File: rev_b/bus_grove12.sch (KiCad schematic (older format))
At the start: 57 parts, among them J1 TERMINATE_JUMPER, J2 LED_CONN_2X2, SW1 MJTP1243, U1 LM2940, U2 74HCT08, U3 MCP2562, U4 74HCT03, U5 ATMEGA328_DIP28, X1 16MHz

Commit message: Rev. B is ready.
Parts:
- C5: value 1uF -> .1uF
- N2: footprint bus_grove12:Pin_Header_Straight_1x06 -> ~
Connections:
- net GND: no longer H1.1 (GND), H2.1 (GND), H3.1 (GND), H4.1 (GND)
- net at R9.2, U4.12, U4.13: now also C7.1, R10.1
- no-connect marks 7 -> 11
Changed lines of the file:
@@
 Sheet 1 2
 Title "Bus Grove 12"
-Date "Sun 02 Nov 2014"
-Rev "A"
+Date "Mon 09 Feb 2015"
+Rev "B"
 Comp ""
 Comment1 ""
@@
 F 0 "N2" H 1050 8100 50  0000 C CNN
 F 1 "FTDI_HEADER" H 1150 7275 50  0000 C CNN
-F 2 "bus_grove12:Pin_Header_Straight_1x06" H 1150 7500 60  0001 C CNN
+F 2 "~" H 1150 7500 60  0000 C CNN
 F 3 "" H 1150 7500 60  0000 C CNN
 	1    1150 7500
@@
 P 4200 6950
 F 0 "C5" H 4260 7010 50  0000 L CNN
-F 1 "1uF" H 4260 6880 50  0000 L CNN
+F 1 ".1uF" H 4260 6880 50  0000 L CNN
 F 2 "bus_grove12:Capacitor4x3RM2-5_RevB" H 4238 6800 30  0001 C CNN
 F 3 "" H 4200 6950 60  0000 C CNN
@@
 	1800 6950 1800 7350
 Wire Wire Line
-	1600 7800 5300 7800
-Wire Wire Line
 	1800 7750 1800 7800
 Connection ~ 1800 7800
@@
 	5100 7400 5000 7400
 Connection ~ 5100 6950
-Wire Wire Line
-	5200 6600 5200 7800
-Wire Wire Line
-	5200 6600 5300 6600
-Wire Wire Line
-	5300 7000 5200 7000
-Connection ~ 5200 7000
-Wire Wire Line
-	5300 7400 5200 7400
-Connection ~ 5200 7400
-Connection ~ 5200 7800
 Wire Wire Line
 	4400 7400 4000 7400
@@
 Wire Wire Line
 	5600 6100 5600 5900
+Connection ~ 5900 1400
+Wire Wire Line
+	1600 7800 4000 7800
+NoConn ~ 5300 6600
+NoConn ~ 5300 7000
+NoConn ~ 5300 7400
+NoConn ~ 5300 7800
 $EndSCHEMATC

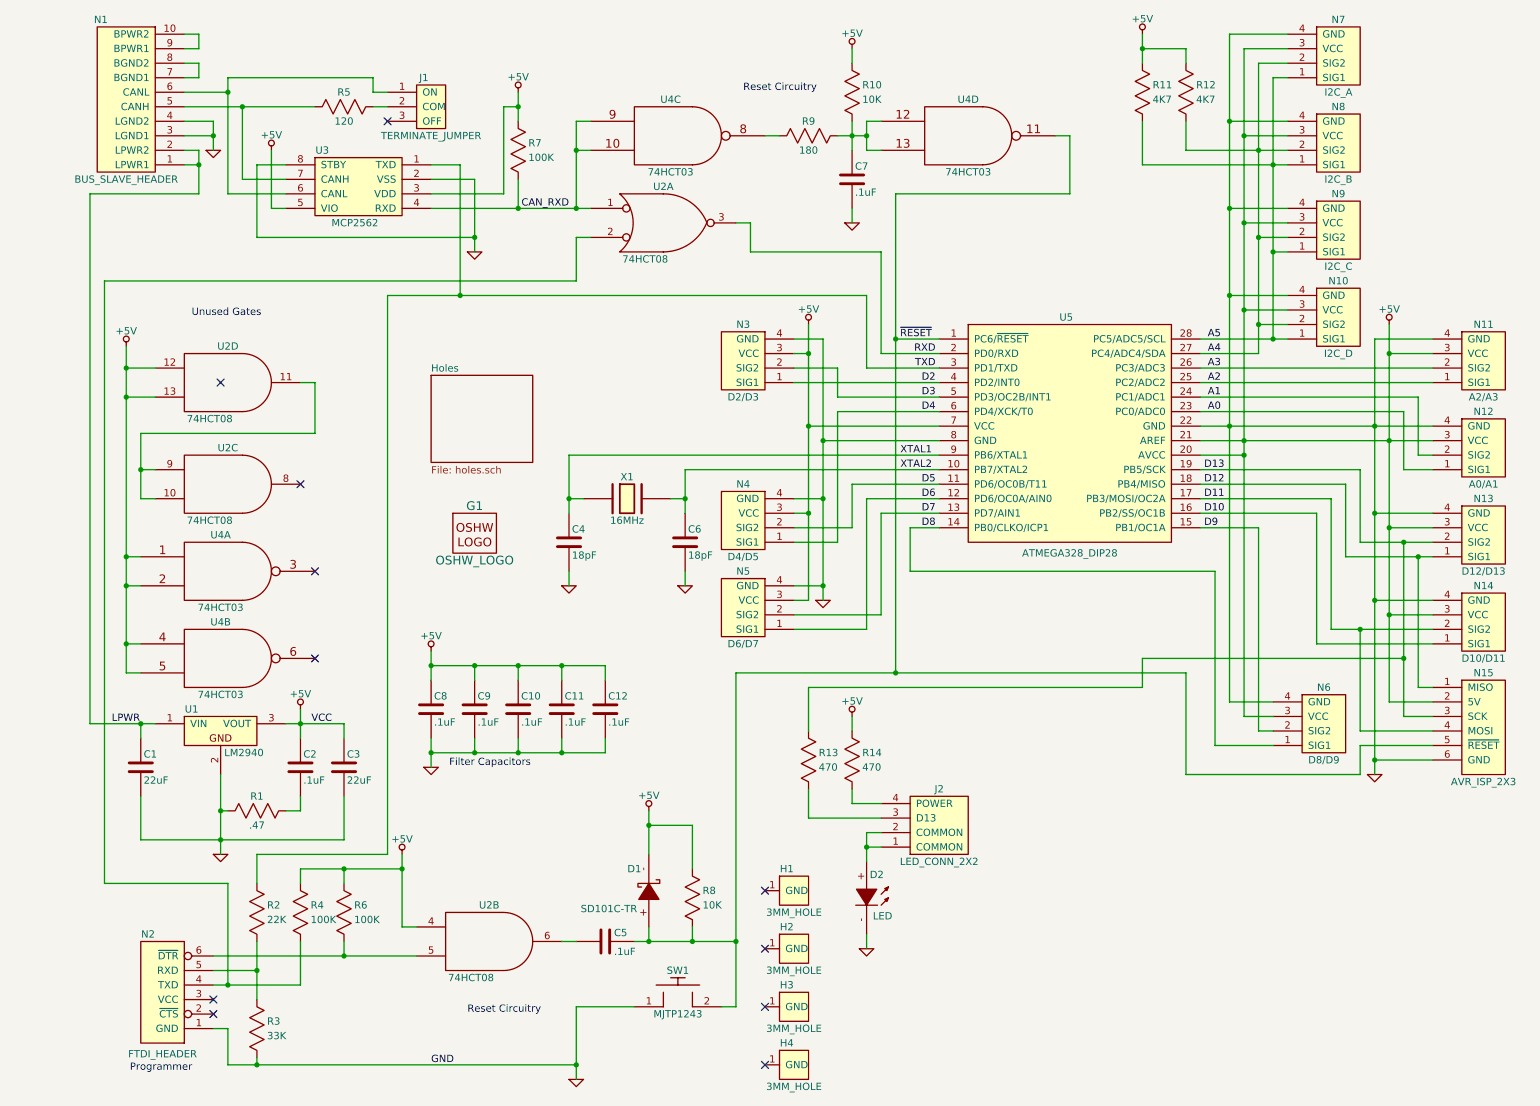
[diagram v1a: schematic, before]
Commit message: Split 22uF capacitor into tantalum and aluminum.
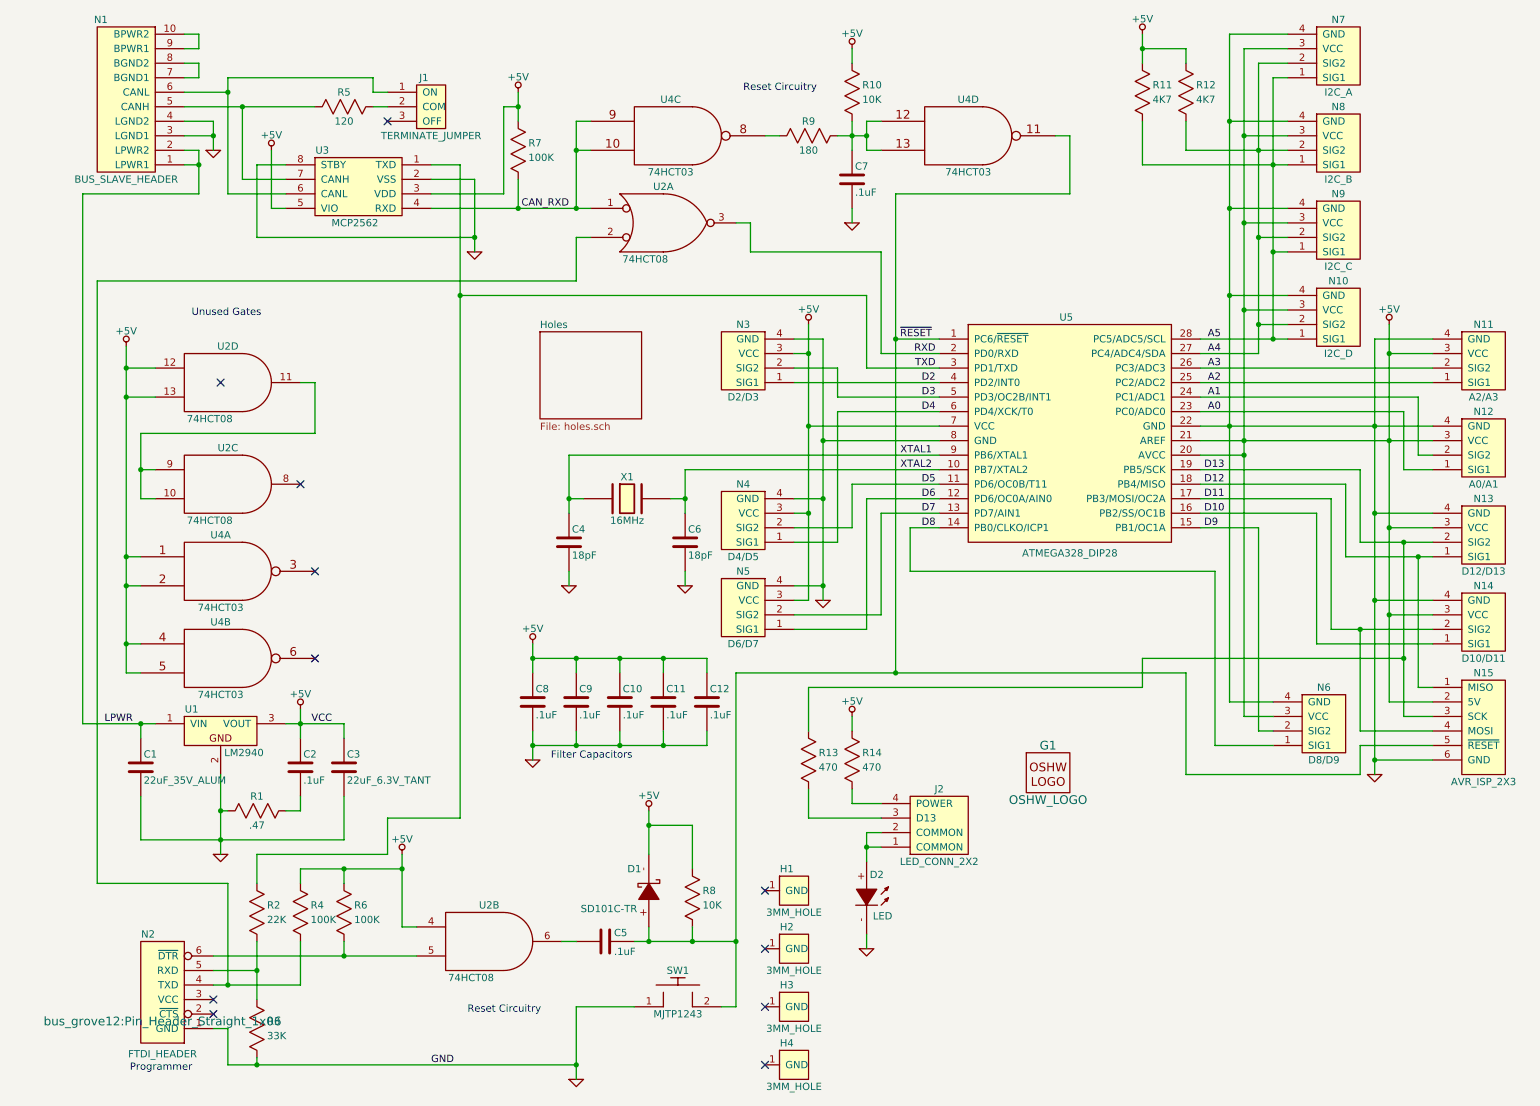
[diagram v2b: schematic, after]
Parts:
- C1: value 22uF -> 22uF_35V_ALUM
- C3: value 22uF -> 22uF_6.3V_TANT
- N2: footprint ~ -> bus_grove12:Pin_Header_Straight_1x06
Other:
- moved on the sheet: C10, C11, C12, C8, C9, G1
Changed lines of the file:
@@
 L OSHW_LOGO G1
 U 1 1 53AA4798
-P 3300 4150
-F 0 "G1" H 3300 4350 60  0000 C CNN
-F 1 "OSHW_LOGO" H 3300 3975 60  0000 C CNN
-F 2 "bus_grove12:OSHW_LOGO_400mil" H 3300 4150 60  0001 C CNN
-F 3 "" H 3300 4150 60  0000 C CNN
-	1    3300 4150
+P 7250 5800
+F 0 "G1" H 7250 6000 60  0000 C CNN
+F 1 "OSHW_LOGO" H 7250 5625 60  0000 C CNN
+F 2 "bus_grove12:OSHW_LOGO_400mil" H 7250 5800 60  0001 C CNN
+F 3 "" H 7250 5800 60  0000 C CNN
+	1    7250 5800
 	1    0    0    -1
 $EndComp
@@
 F 0 "N2" H 1050 8100 50  0000 C CNN
 F 1 "FTDI_HEADER" H 1150 7275 50  0000 C CNN
-F 2 "~" H 1150 7500 60  0000 C CNN
+F 2 "bus_grove12:Pin_Header_Straight_1x06" H 1150 7500 60  0000 C CNN
 F 3 "" H 1150 7500 60  0000 C CNN
 	1    1150 7500
@@
 P 1000 5750
 F 0 "C1" H 1020 5840 50  0000 L CNN
-F 1 "22uF" H 1020 5660 50  0000 L CNN
+F 1 "22uF_35V_ALUM" H 1020 5660 50  0000 L CNN
 F 2 "bus_grove12:Capacitor3MMDiscRM2.5" H 1038 5600 30  0001 C CNN
 F 3 "" H 1000 5750 60  0000 C CNN
@@
 P 2400 5750
 F 0 "C3" H 2420 5840 50  0000 L CNN
-F 1 "22uF" H 2420 5660 50  0000 L CNN
+F 1 "22uF_6.3V_TANT" H 2420 5660 50  0000 L CNN
 F 2 "bus_grove12:Capacitor3MMDiscRM2.5" H 2438 5600 30  0001 C CNN
 F 3 "" H 2400 5750 60  0000 C CNN
@@
 L C_VERT C8
 U 1 1 53EA3930
-P 3000 5350
-F 0 "C8" H 3020 5440 50  0000 L CNN
-F 1 ".1uF" H 3020 5260 50  0000 L CNN
-F 2 "bus_grove12:Capacitor4x3RM2-5_RevB" H 3038 5200 30  0001 C CNN
-F 3 "" H 3000 5350 60  0000 C CNN
-	1    3000 5350
+P 3700 5300
+F 0 "C8" H 3720 5390 50  0000 L CNN
+F 1 ".1uF" H 3720 5210 50  0000 L CNN
+F 2 "bus_grove12:Capacitor4x3RM2-5_RevB" H 3738 5150 30  0001 C CNN
+F 3 "" H 3700 5300 60  0000 C CNN
+	1    3700 5300
 	1    0    0    -1
 $EndComp
@@
 L C_VERT C9
 U 1 1 53EA3BB3
-P 3300 5350
-F 0 "C9" H 3320 5440 50  0000 L CNN
-F 1 ".1uF" H 3320 5260 50  0000 L CNN
-F 2 "bus_grove12:Capacitor4x3RM2-5_RevB" H 3338 5200 30  0001 C CNN
-F 3 "" H 3300 5350 60  0000 C CNN
-	1    3300 5350
+P 4000 5300
+F 0 "C9" H 4020 5390 50  0000 L CNN
+F 1 ".1uF" H 4020 5210 50  0000 L CNN
+F 2 "bus_grove12:Capacitor4x3RM2-5_RevB" H 4038 5150 30  0001 C CNN
+F 3 "" H 4000 5300 60  0000 C CNN
+	1    4000 5300
 	1    0    0    -1
 $EndComp
@@
 L C_VERT C10
 U 1 1 53EA3C1E
-P 3600 5350
-F 0 "C10" H 3620 5440 50  0000 L CNN
-F 1 ".1uF" H 3620 5260 50  0000 L CNN
-F 2 "bus_grove12:Capacitor4x3RM2-5_RevB" H 3638 5200 30  0001 C CNN
-F 3 "" H 3600 5350 60  0000 C CNN
-	1    3600 5350
+P 4300 5300
+F 0 "C10" H 4320 5390 50  0000 L CNN
+F 1 ".1uF" H 4320 5210 50  0000 L CNN
+F 2 "bus_grove12:Capacitor4x3RM2-5_RevB" H 4338 5150 30  0001 C CNN
+F 3 "" H 4300 5300 60  0000 C CNN
+	1    4300 5300
 	1    0    0    -1
 $EndComp
@@
 L C_VERT C11
 U 1 1 53EA3C8A
-P 3900 5350
-F 0 "C11" H 3920 5440 50  0000 L CNN
-F 1 ".1uF" H 3920 5260 50  0000 L CNN
-F 2 "bus_grove12:Capacitor4x3RM2-5_RevB" H 3938 5200 30  0001 C CNN
-F 3 "" H 3900 5350 60  0000 C CNN
-	1    3900 5350
+P 4600 5300
+F 0 "C11" H 4620 5390 50  0000 L CNN
+F 1 ".1uF" H 4620 5210 50  0000 L CNN
+F 2 "bus_grove12:Capacitor4x3RM2-5_RevB" H 4638 5150 30  0001 C CNN
+F 3 "" H 4600 5300 60  0000 C CNN
+	1    4600 5300
 	1    0    0    -1
 $EndComp
@@
 L +5V #PWR012
 U 1 1 53EA3CF1
-P 3000 4950
-F 0 "#PWR012" H 3000 5040 20  0001 C CNN
-F 1 "+5V" H 3000 5055 50  0000 C CNN
-F 2 "" H 3000 4950 60  0000 C CNN
-F 3 "" H 3000 4950 60  0000 C CNN
-	1    3000 4950
+P 3700 4900
+F 0 "#PWR012" H 3700 4990 20  0001 C CNN
+F 1 "+5V" H 3700 5005 50  0000 C CNN
+F 2 "" H 3700 4900 60  0000 C CNN
+F 3 "" H 3700 4900 60  0000 C CNN
+	1    3700 4900
 	1    0    0    -1
 $EndComp
@@
 L GND #PWR013
 U 1 1 53EA3DE7
-P 3000 5750
-F 0 "#PWR013" H 3000 5750 30  0001 C CNN
-F 1 "GND" H 3000 5680 30  0001 C CNN
-F 2 "" H 3000 5750 60  0000 C CNN
-F 3 "" H 3000 5750 60  0000 C CNN
-	1    3000 5750
-	1    0    0    -1
-$EndComp
-Text Notes 3125 5750 0    50   ~ 0
+P 3700 5700
+F 0 "#PWR013" H 3700 5700 30  0001 C CNN
+F 1 "GND" H 3700 5630 30  0001 C CNN
+F 2 "" H 3700 5700 60  0000 C CNN
+F 3 "" H 3700 5700 60  0000 C CNN
+	1    3700 5700
+	1    0    0    -1
+$EndComp
+Text Notes 3825 5700 0    50   ~ 0
 Filter Capacitors
 Text Notes 3250 7450 0    50   ~ 0
@@
 Text Notes 925  7850 0    50   ~ 0
 Programmer
-Text Label 800  5450 0    50   ~ 0
+Text Label 750  5450 0    50   ~ 0
 LPWR
 Text Label 6475 3200 2    50   ~ 0
@@
 L C_VERT C12
 U 1 1 53F15832
-P 4200 5350
-F 0 "C12" H 4220 5440 50  0000 L CNN
-F 1 ".1uF" H 4220 5260 50  0000 L CNN
-F 2 "bus_grove12:Capacitor4x3RM2-5_RevB" H 4238 5200 30  0001 C CNN
-F 3 "" H 4200 5350 60  0000 C CNN
-	1    4200 5350
+P 4900 5300
+F 0 "C12" H 4920 5390 50  0000 L CNN
+F 1 ".1uF" H 4920 5210 50  0000 L CNN
+F 2 "bus_grove12:Capacitor4x3RM2-5_RevB" H 4938 5150 30  0001 C CNN
+F 3 "" H 4900 5300 60  0000 C CNN
+	1    4900 5300
 	1    0    0    -1
 $EndComp
@@
 $EndComp
 $Sheet
-S 3000 3050 700  600
+S 3750 2750 700  600
 U 545698AF
 F0 "Holes" 50
@@
 Connection ~ 1000 5450
 Wire Wire Line
-	650  5450 1100 5450
+	600  5450 1100 5450
 Wire Wire Line
 	1000 5550 1000 5450
@@
 Connection ~ 1400 1600
 Wire Wire Line
-	650  1800 650  5450
-Wire Wire Line
-	1400 1800 650  1800
+	600  1800 600  5450
+Wire Wire Line
+	1400 1800 600  1800
 Connection ~ 1500 1400
 Wire Wire Line
@@
 	1600 7250 1600 6550
 Wire Wire Line
-	1600 6550 750  6550
-Wire Wire Line
-	750  6550 750  2400
-Wire Wire Line
-	750  2400 4000 2400
+	1600 6550 700  6550
+Wire Wire Line
+	700  6550 700  2400
+Wire Wire Line
+	700  2400 4000 2400
 Wire Wire Line
 	2100 6550 2100 6450
@@
 Wire Wire Line
 	2800 6850 2900 6850
-Wire Wire Line
-	2700 2500 2700 6350
 Wire Wire Line
 	2700 6350 1800 6350
@@
 	1800 1600 1800 2100
 Wire Wire Line
-	3000 4950 3000 5150
-Wire Wire Line
-	3000 5050 4200 5050
-Wire Wire Line
-	3900 5050 3900 5150
-Connection ~ 3000 5050
-Wire Wire Line
-	3600 5150 3600 5050
-Connection ~ 3600 5050
-Wire Wire Line
-	3300 5150 3300 5050
-Connection ~ 3300 5050
-Wire Wire Line
-	3000 5550 3000 5750
-Wire Wire Line
-	3000 5650 4200 5650
-Wire Wire Line
-	3900 5650 3900 5550
-Connection ~ 3000 5650
-Wire Wire Line
-	3600 5550 3600 5650
-Connection ~ 3600 5650
-Wire Wire Line
-	3300 5550 3300 5650
-Connection ~ 3300 5650
+	3700 4900 3700 5100
+Wire Wire Line
+	3700 5000 4900 5000
+Wire Wire Line
+	4600 5000 4600 5100
+Connection ~ 3700 5000
+Wire Wire Line
+	4300 5100 4300 5000
+Connection ~ 4300 5000
+Wire Wire Line
+	4000 5100 4000 5000
+Connection ~ 4000 5000
+Wire Wire Line
+	3700 5500 3700 5700
+Wire Wire Line
+	3700 5600 4900 5600
+Wire Wire Line
+	4600 5600 4600 5500
+Connection ~ 3700 5600
+Wire Wire Line
+	4300 5500 4300 5600
+Connection ~ 4300 5600
+Wire Wire Line
+	4000 5500 4000 5600
+Connection ~ 4000 5600
 Wire Wire Line
 	1300 1000 1400 1000
@@
 	2100 7250 2100 6950
 Wire Wire Line
-	4200 5050 4200 5150
-Connection ~ 3900 5050
-Wire Wire Line
-	4200 5650 4200 5550
-Connection ~ 3900 5650
-Wire Wire Line
-	3200 1600 3200 2500
+	4900 5000 4900 5100
+Connection ~ 4600 5000
+Wire Wire Line
+	4900 5600 4900 5500
+Connection ~ 4600 5600
+Wire Wire Line
+	3200 1600 3200 6100
 Wire Wire Line
 	3000 1600 3200 1600
@@
 	9100 4000 8300 4000
 Wire Wire Line
-	9900 5400 9700 5400
-Wire Wire Line
-	9700 5400 9700 4200
+	9700 5400 9900 5400
+Wire Wire Line
+	9700 4200 9700 5400
 Connection ~ 9700 4200
 Wire Wire Line
@@
 	6500 3000 6000 3000
 Wire Wire Line
-	6000 3000 6000 2500
-Wire Wire Line
-	6000 2500 2700 2500
+	6000 2500 6000 3000
 Wire Wire Line
 	4100 2100 4000 2100
@@
 NoConn ~ 5300 7400
 NoConn ~ 5300 7800
+Wire Wire Line
+	2700 6350 2700 6100
+Wire Wire Line
+	2700 6100 3200 6100
+Wire Wire Line
+	3200 2500 6000 2500
 $EndSCHEMATC
